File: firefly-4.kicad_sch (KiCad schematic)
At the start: 0 parts

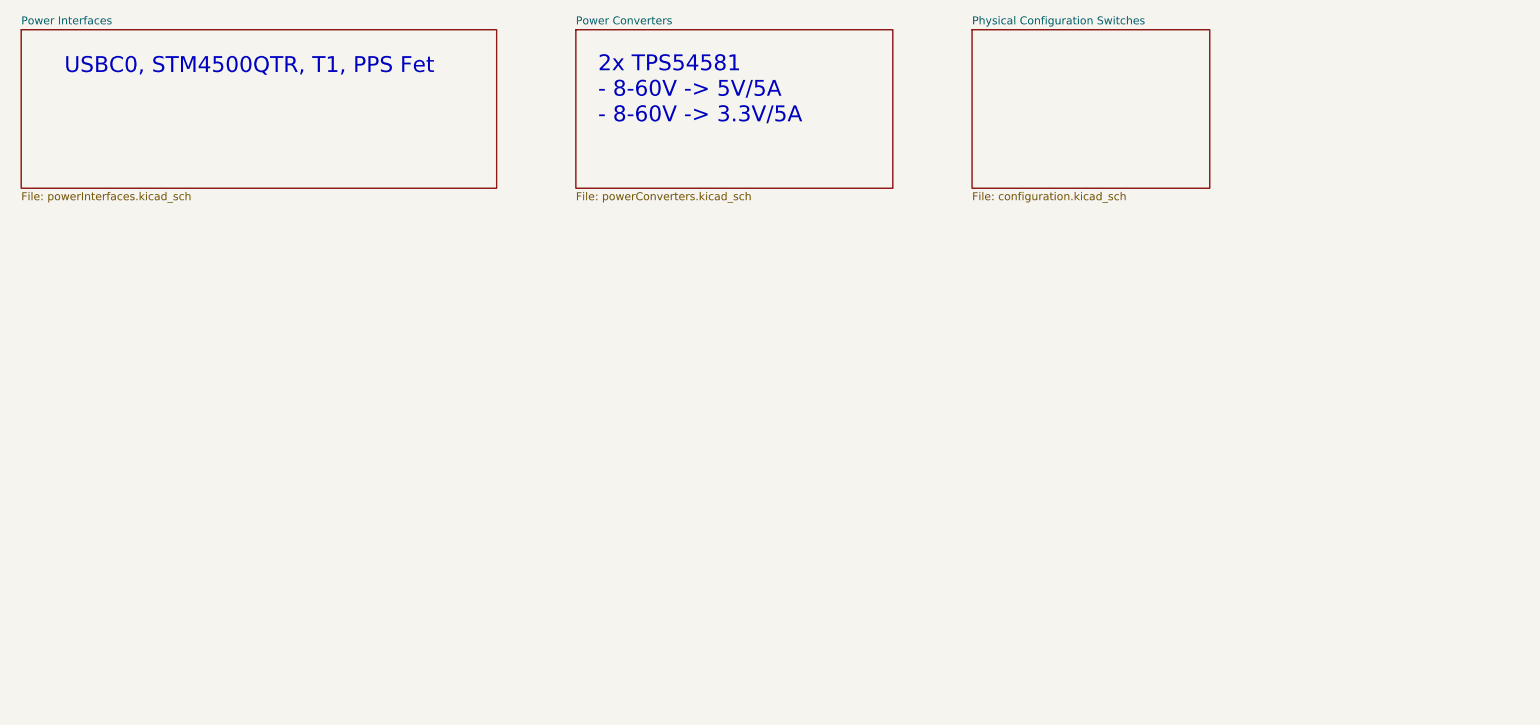
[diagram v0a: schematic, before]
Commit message: Complete schematic transfer
Signed-off-by: Matthew Guo <matthew@botbuilt.com>
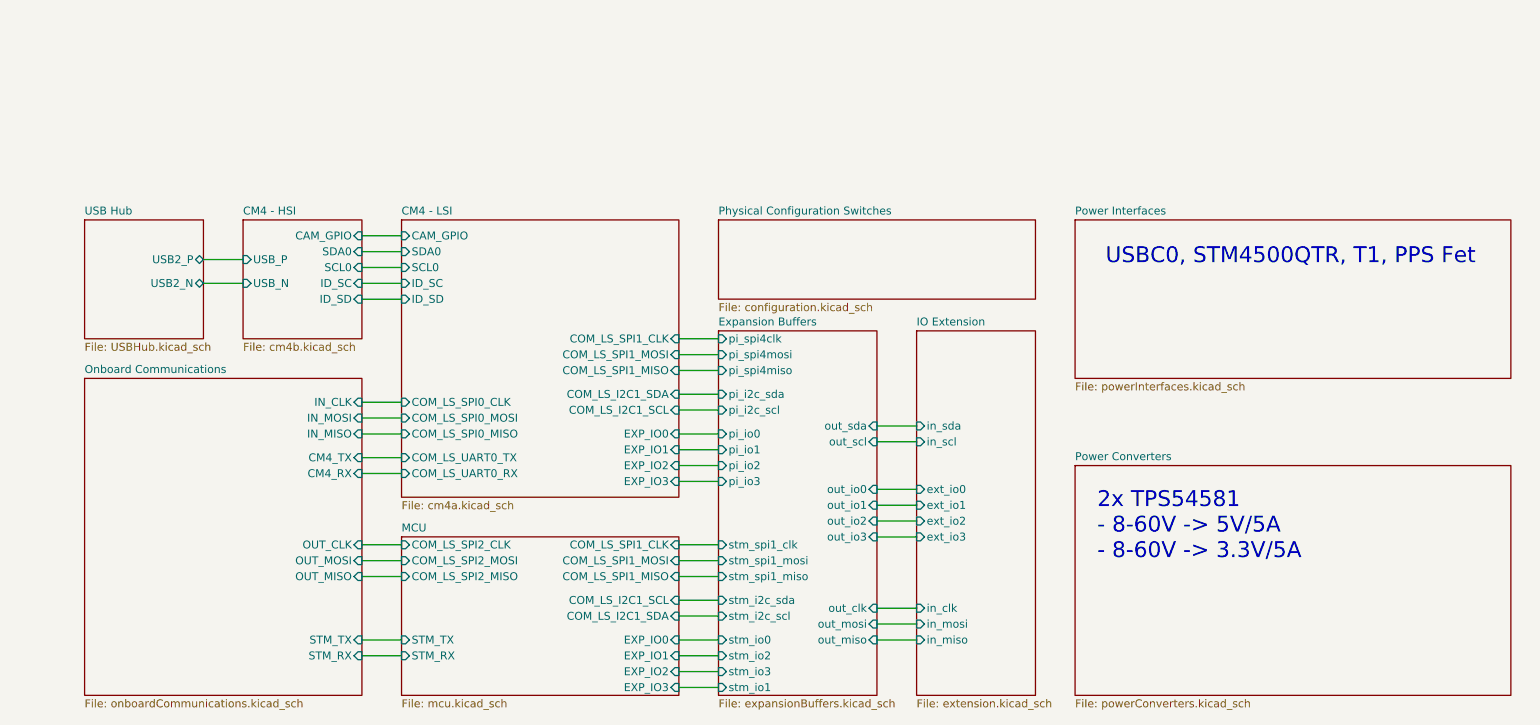
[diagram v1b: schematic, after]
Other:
- added sheet CM4 - HSI (cm4b.kicad_sch)
- added sheet CM4 - LSI (cm4a.kicad_sch)
- added sheet Expansion Buffers (expansionBuffers.kicad_sch)
- added sheet IO Extension (extension.kicad_sch)
- added sheet MCU (mcu.kicad_sch)
- added sheet Onboard Communications (onboardCommunications.kicad_sch)
- added sheet USB Hub (USBHub.kicad_sch)
